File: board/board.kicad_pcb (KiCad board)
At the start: 2 copper layers, 45 x 29 mm, 31 parts, among them J1 002_SPI, J2 Conn_01x02_Male, J3 019_100BASE-T_with_CT, U1 W5500, Y1 25MHz

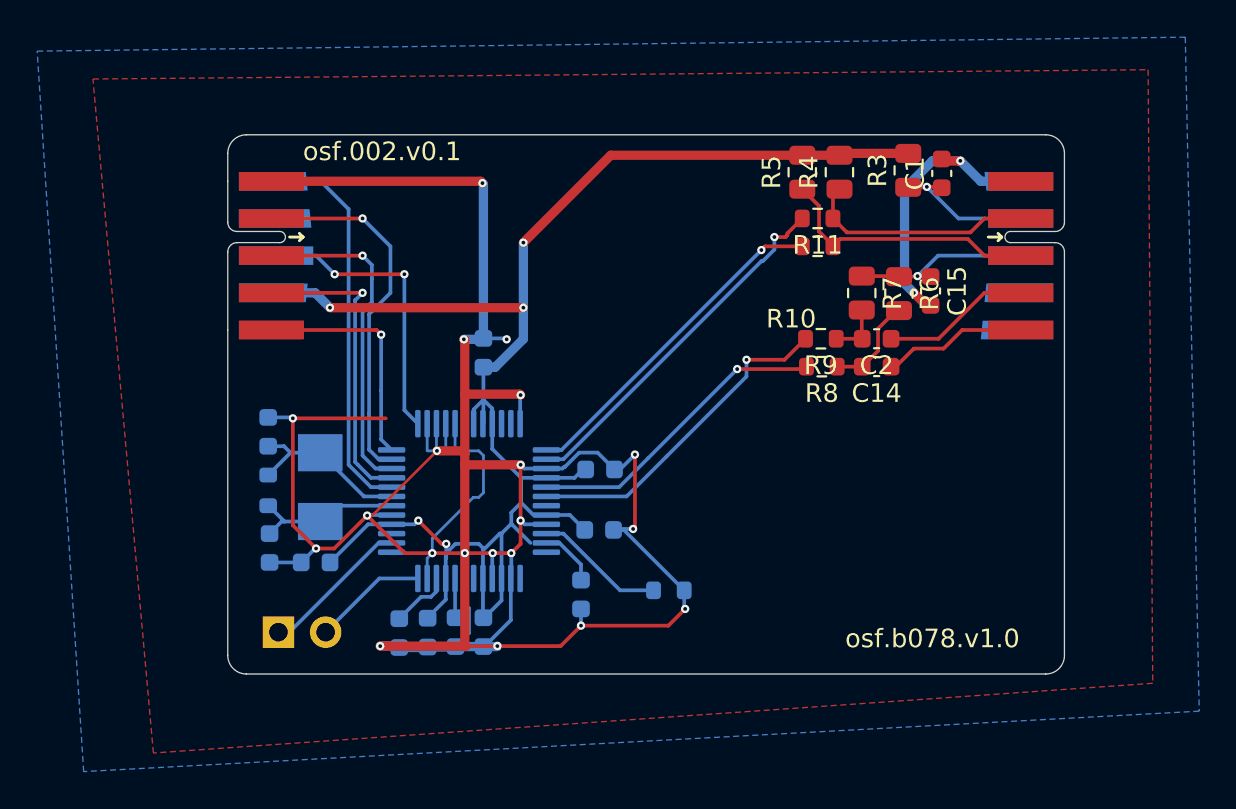
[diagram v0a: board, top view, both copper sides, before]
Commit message: broke out all leds in external connector
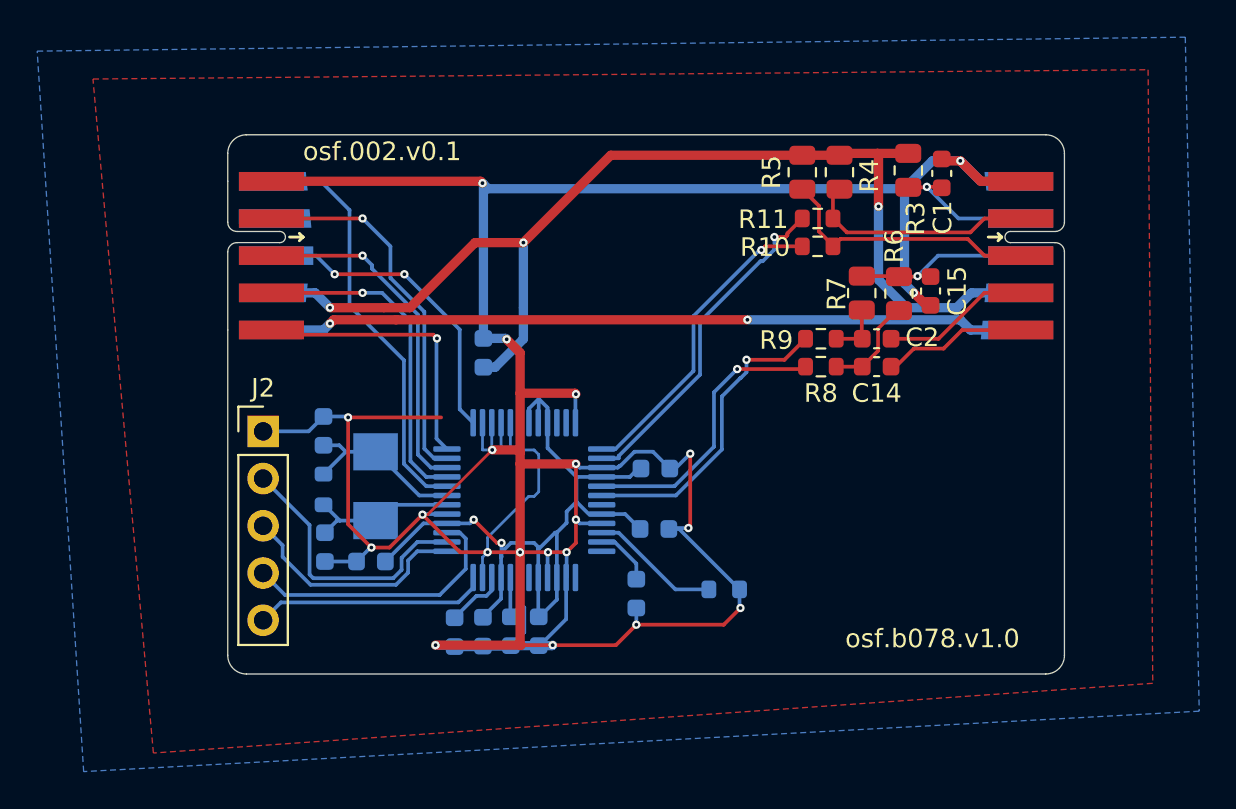
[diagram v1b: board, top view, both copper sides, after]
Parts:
- J2: value Conn_01x02_Male -> Conn_01x05_Male; footprint Connector_PinHeader_2.54mm:PinHeader_1x02_P2.54mm_Vertical -> Connector_PinHeader_2.54mm:PinHeader_1x05_P2.54mm_Vertical; moved to F.Cu
- moved J2 10.8 mm to (78.9, 90.0), turned to 0 degrees
- moved C10 2.98 mm to (89.2, 100.8)
- moved C12 2.98 mm to (82.2, 89.9)
- moved C5 2.98 mm to (84.7, 97.0)
- moved C7 2.98 mm to (100.0, 95.2)
- moved R1 2.98 mm to (103.7, 98.5)
- moved R2 2.98 mm to (82.2, 93.1)
- moved U1 2.98 mm to (93.0, 93.7)
- moved Y1 2.98 mm to (85.0, 92.9)
- moved C11 2.98 mm to (92.2, 100.7)
- moved C13 2.98 mm to (82.2, 96.2)
- moved C4 2.98 mm to (100.0, 92.0)
- moved C6 2.98 mm to (90.7, 100.7)
- moved C8 2.98 mm to (93.7, 100.7)
- moved C9 2.98 mm to (99.0, 98.7)
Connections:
- C3 pad 1: +3V3 -> +3.3V
- C4 pad 1: +3V3 -> +3.3V
- C5 pad 1: +3V3 -> +3.3V
- C6 pad 1: +3V3 -> +3.3V
- C7 pad 1: +3V3 -> +3.3V
- C8 pad 1: +3V3 -> +3.3V
- C9 pad 1: +3V3 -> +3.3V
- J1 pad 10: unconnected-(J1-Pad10) -> Net-(J3-Pad10)
- J1 pad 9: +3V3 -> +3.3V
- J2 pad 1: /controller/DUPLED -> GND
- J2 pad 2: /controller/SPDLED -> /DUPLED
- J3 pad 10: (no net) -> Net-(J3-Pad10)
- J3 pad 9: (no net) -> +3.3V
- R3 pad 2: +3V3 -> +3.3V
- R4 pad 2: +3V3 -> +3.3V
- R5 pad 2: +3V3 -> +3.3V
- U1 pad 11: +3V3 -> +3.3V
- U1 pad 15: +3V3 -> +3.3V
- U1 pad 17: +3V3 -> +3.3V
- U1 pad 21: +3V3 -> +3.3V
- U1 pad 24: /controller/SPDLED -> /SPDLED
- U1 pad 26: /controller/DUPLED -> /DUPLED
- U1 pad 28: +3V3 -> +3.3V
- U1 pad 4: +3V3 -> +3.3V
- U1 pad 43: +3V3 -> +3.3V
- U1 pad 44: +3V3 -> +3.3V
- U1 pad 45: +3V3 -> +3.3V
- U1 pad 8: +3V3 -> +3.3V
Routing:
- net +3.3V: track 0.00 -> 107.7 mm, vias 0 -> 5
- net +3V3: track 94.0 -> 0.00 mm, vias 5 -> 0
- net Net-(J3-Pad10): track 0.00 -> 40.7 mm, vias 0 -> 2
- net GND: track 182.8 -> 210.5 mm, vias 22 -> 21
- net /DUPLED: track 0.00 -> 14.9 mm
- net /ACTLED: track 0.00 -> 14.7 mm
- net /LINKLED: track 0.00 -> 12.7 mm
- net /SPDLED: track 0.00 -> 12.6 mm
- net /controller/DUPLED: track 8.08 -> 0.00 mm
- net /controller/SPDLED: track 6.16 -> 0.00 mm
- net /controller/INT: track 12.4 -> 15.3 mm
- net /controller/SCLK: track 16.5 -> 17.9 mm
- net Net-(R9-Pad2): track 18.0 -> 16.5 mm
- net Net-(R8-Pad2): track 16.7 -> 15.4 mm
- net Net-(R10-Pad2): track 18.3 -> 17.0 mm
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- added copper zone on B.Cu, net +3.3V
- removed copper zone on B.Cu, net +3V3

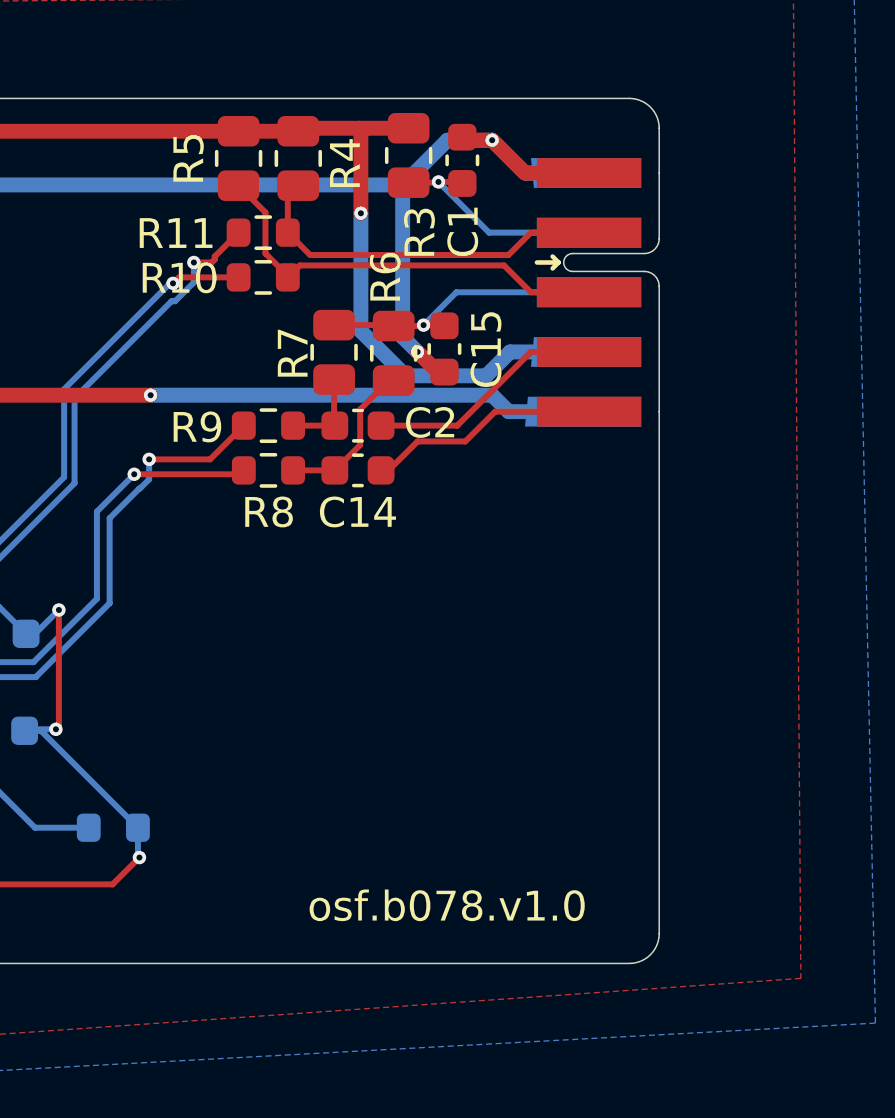
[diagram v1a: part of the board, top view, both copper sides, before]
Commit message: added option for shorted center taps
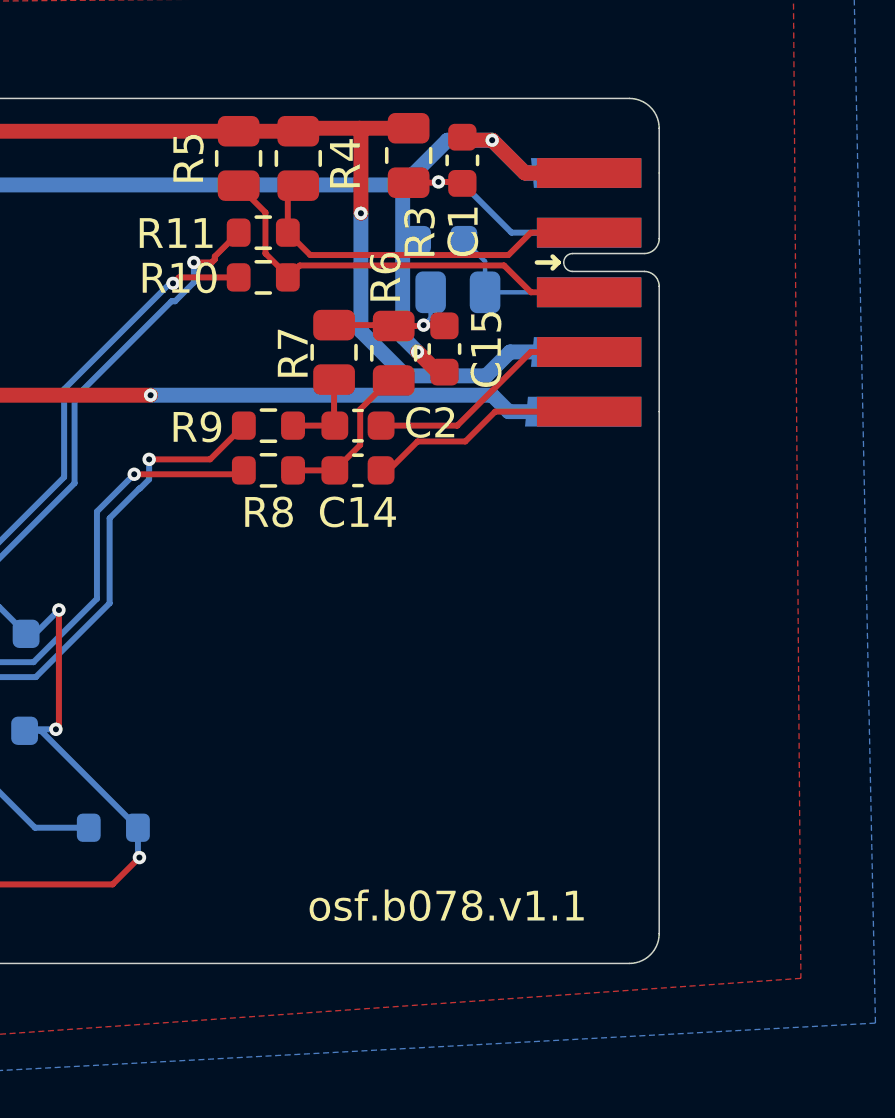
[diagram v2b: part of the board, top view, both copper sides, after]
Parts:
- added C16: 100nF, Capacitor_SMD:C_0603_1608Metric, B.Cu at (114.7, 78.8)
- added R12: d.n.p, Resistor_SMD:R_0805_2012Metric, B.Cu at (115.2, 80.5)
- C1: value 22nF -> 100nF
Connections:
- C15 pad 1: /controller/CT2 -> Net-(C15-Pad1)
- R6 pad 1: /controller/CT2 -> Net-(C15-Pad1)
- R7 pad 1: /controller/CT2 -> Net-(C15-Pad1)
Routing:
- net Net-(C15-Pad1): track 0.00 -> 4.93 mm, vias 0 -> 1
- net /controller/CT2: track 9.74 -> 5.53 mm, vias 1 -> 0
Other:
- board text added: "osf.b078.v1.1"
- board text removed: "osf.b078.v1.0"
